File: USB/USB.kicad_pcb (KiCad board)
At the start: 4 copper layers, 70 x 60 mm, 24 parts, among them J1 USBC-4-0-CX90MW9-24P1, U2 ESDA25L, U3 USB SWITCH 2CHANNEL TS3USB221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, U6 usb-polarity-TUSB321RWBR

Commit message: actually connect the test points (DUMBASS)
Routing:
- net MUX POL: track 11.3 -> 108.6 mm
- net USB SWITCH: track 0.00 -> 21.2 mm
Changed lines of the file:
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@@
 	)
 	(segment
+		(start 96.1235 109.5735)
+		(end 85.925 99.375)
+		(width 0.2)
+		(layer "F.Cu")
+		(net "MUX POL")
+	)
+	(segment
+		(start 103.7 75.125)
+		(end 107.79 79.215)
+		(width 0.2)
+		(layer "F.Cu")
+		(net "MUX POL")
+	)
+	(segment
+		(start 89.85 75.125)
+		(end 103.7 75.125)
+		(width 0.2)
+		(layer "F.Cu")
+		(net "MUX POL")
+	)
+	(segment
+		(start 120.63 109.5735)
+		(end 96.1235 109.5735)
+		(width 0.2)
+		(layer "F.Cu")
+		(net "MUX POL")
+	)
+	(segment
 		(start 110.04 92.354857)
 		(end 110.04 91.910001)
@@
 	)
 	(segment
+		(start 85.925 79.05)
+		(end 89.85 75.125)
+		(width 0.2)
+		(layer "F.Cu")
+		(net "MUX POL")
+	)
+	(segment
 		(start 109.756811 92.951)
 		(end 109.081 92.951)
@@
 	)
 	(segment
+		(start 107.79 79.215)
+		(end 107.79 92.15)
+		(width 0.2)
+		(layer "F.Cu")
+		(net "MUX POL")
+	)
+	(segment
 		(start 110.09807 92.412927)
 		(end 110.09807 92.609741)
@@
 		(net "MUX POL")
 	)
+	(segment
+		(start 85.925 99.375)
+		(end 85.925 79.05)
+		(width 0.2)
+		(layer "F.Cu")
+		(net "MUX POL")
+	)
 	(via
 		(at 117.19 92.88)
@@
 		(net "RX1+")
 	)
+	(segment
+		(start 116.8326 99.000001)
+		(end 115.693801 99.000001)
+		(width 0.2)
+		(layer "F.Cu")
+		(net "USB SWITCH")
+	)
+	(segment
+		(start 123.17 101.280199)
+		(end 123.17 109.5735)
+		(width 0.2)
+		(layer "F.Cu")
+		(net "USB SWITCH")
+	)
+	(segment
+		(start 115.405197 98.711397)
+		(end 115.405197 97.738407)
+		(width 0.2)
+		(layer "F.Cu")
+		(net "USB SWITCH")
+	)
+	(segment
+		(start 115.405197 97.738407)
+		(end 116.843604 96.3)
+		(width 0.2)
+		(layer "F.Cu")
+		(net "USB SWITCH")
+	)
+	(segment
+		(start 118.189801 96.3)
+		(end 123.17 101.280199)
+		(width 0.2)
+		(layer "F.Cu")
+		(net "USB SWITCH")
+	)
+	(segment
+		(start 115.693801 99.000001)
+		(end 115.405197 98.711397)
+		(width 0.2)
+		(layer "F.Cu")
+		(net "USB SWITCH")
+	)
+	(segment
+		(start 116.843604 96.3)
+		(end 118.189801 96.3)
+		(width 0.2)
+		(layer "F.Cu")
+		(net "USB SWITCH")
+	)
 	(zone

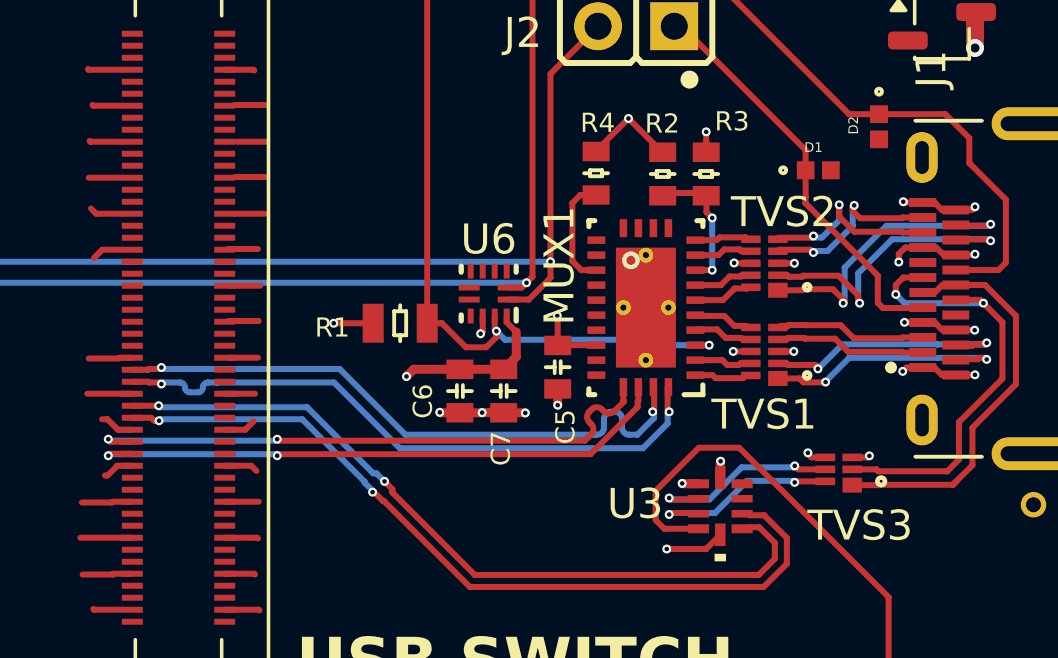
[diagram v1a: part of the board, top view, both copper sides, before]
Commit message: stitching vias along SS lines
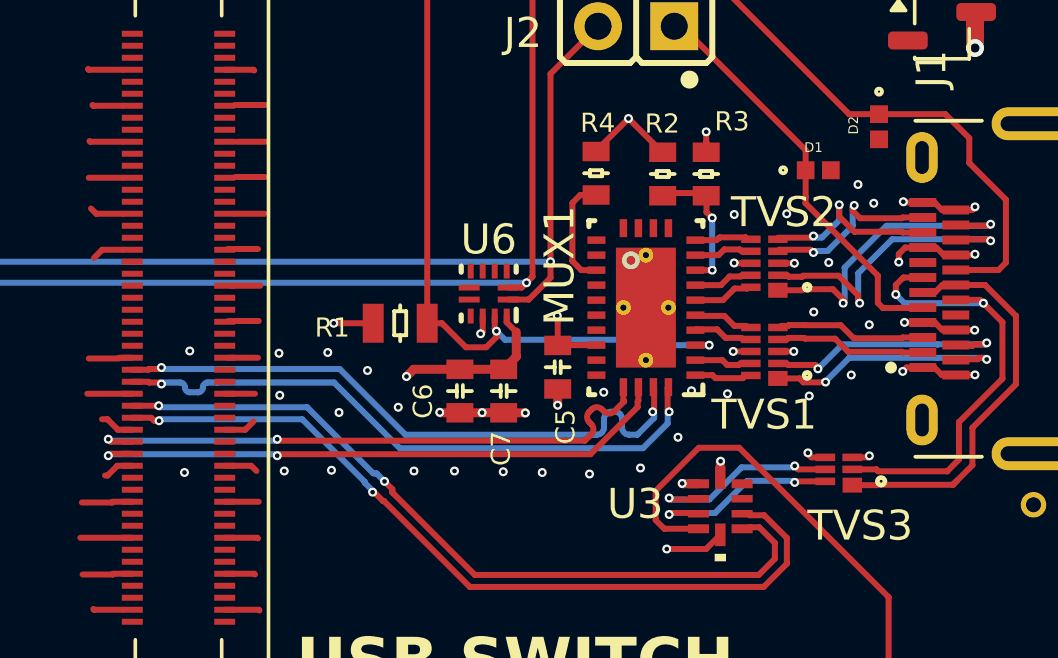
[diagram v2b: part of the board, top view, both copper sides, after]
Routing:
- net GND: vias 18 -> 47
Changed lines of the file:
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@@
+	)
+	(via
+		(at 122.525 92.2)
+		(size 0.3)
+		(drill 0.15)
+		(layers "F.Cu" "B.Cu")
+		(free yes)
+		(net "GND")
 	)
 	(via
@@
 	)
 	(via
+		(at 104.6 97.05)
+		(size 0.3)
+		(drill 0.15)
+		(layers "F.Cu" "B.Cu")
+		(free yes)
+		(net "GND")
+	)
+	(via
+		(at 113.2 97.175)
+		(size 0.3)
+		(drill 0.15)
+		(layers "F.Cu" "B.Cu")
+		(free yes)
+		(net "GND")
+	)
+	(via
+		(at 104.475 93.125)
+		(size 0.3)
+		(drill 0.15)
+		(layers "F.Cu" "B.Cu")
+		(free yes)
+		(net "GND")
+	)
+	(via
+		(at 114.9 96.975)
+		(size 0.3)
+		(drill 0.15)
+		(layers "F.Cu" "B.Cu")
+		(free yes)
+		(net "GND")
+	)
+	(via
+		(at 120.525 94.575)
+		(size 0.3)
+		(drill 0.15)
+		(layers "F.Cu" "B.Cu")
+		(free yes)
+		(net "GND")
+	)
+	(via
+		(at 110.325 97.1)
+		(size 0.3)
+		(drill 0.15)
+		(layers "F.Cu" "B.Cu")
+		(free yes)
+		(net "GND")
+	)
+	(via
+		(at 116.6 94.4)
+		(size 0.3)
+		(drill 0.15)
+		(layers "F.Cu" "B.Cu")
+		(free yes)
+		(net "GND")
+	)
+	(via
+		(at 104.85 95.125)
+		(size 0.3)
+		(drill 0.15)
+		(layers "F.Cu" "B.Cu")
+		(free yes)
+		(net "GND")
+	)
+	(via
+		(at 102.875 94.55)
+		(size 0.3)
+		(drill 0.15)
+		(layers "F.Cu" "B.Cu")
+		(free yes)
+		(net "GND")
+	)
+	(via
 		(at 118.02 90.14)
 		(size 0.3)
@@
 		)
 		(filling no)
+		(net "GND")
+	)
+	(via
+		(at 116.15 95.95)
+		(size 0.3)
+		(drill 0.15)
+		(layers "F.Cu" "B.Cu")
+		(free yes)
 		(net "GND")
 	)
@@
 	)
 	(via
+		(at 99.875 93.075)
+		(size 0.3)
+		(drill 0.15)
+		(layers "F.Cu" "B.Cu")
+		(free yes)
+		(net "GND")
+	)
+	(via
 		(at 117.99 93.09)
 		(size 0.3)
@@
 	)
 	(via
+		(at 106.825 94.95)
+		(size 0.3)
+		(drill 0.15)
+		(layers "F.Cu" "B.Cu")
+		(free yes)
+		(net "GND")
+	)
+	(via
 		(at 109.57 92.5)
 		(size 0.3)
@@
 		)
 		(filling no)
+		(net "GND")
+	)
+	(via
+		(at 119.775 88.5)
+		(size 0.3)
+		(drill 0.15)
+		(layers "F.Cu" "B.Cu")
+		(free yes)
+		(net "GND")
+	)
+	(via
+		(at 113.675 94.45)
+		(size 0.3)
+		(drill 0.15)
+		(layers "F.Cu" "B.Cu")
+		(free yes)
+		(net "GND")
+	)
+	(via
+		(at 122.675 88.15)
+		(size 0.3)
+		(drill 0.15)
+		(layers "F.Cu" "B.Cu")
+		(free yes)
 		(net "GND")
 	)
@@
 	)
 	(via
+		(at 103.025 97.075)
+		(size 0.3)
+		(drill 0.15)
+		(layers "F.Cu" "B.Cu")
+		(free yes)
+		(net "GND")
+	)
+	(via
+		(at 121.925 93.875)
+		(size 0.3)
+		(drill 0.15)
+		(layers "F.Cu" "B.Cu")
+		(free yes)
+		(net "GND")
+	)
+	(via
+		(at 99.7 97.125)
+		(size 0.3)
+		(drill 0.15)
+		(layers "F.Cu" "B.Cu")
+		(free yes)
+		(net "GND")
+	)
+	(via
+		(at 105.8 93.725)
+		(size 0.3)
+		(drill 0.15)
+		(layers "F.Cu" "B.Cu")
+		(free yes)
+		(net "GND")
+	)
+	(via
+		(at 120.675 91.775)
+		(size 0.3)
+		(drill 0.15)
+		(layers "F.Cu" "B.Cu")
+		(free yes)
+		(net "GND")
+	)
+	(via
+		(at 118.025 88.525)
+		(size 0.3)
+		(drill 0.15)
+		(layers "F.Cu" "B.Cu")
+		(free yes)
+		(net "GND")
+	)
+	(via
+		(at 108.7 97.075)
+		(size 0.3)
+		(drill 0.15)
+		(layers "F.Cu" "B.Cu")
+		(free yes)
+		(net "GND")
+	)
+	(via
 		(at 116.29 97.49)
 		(size 0.3)
@@
 	)
 	(via
+		(at 102.85 93.15)
+		(size 0.3)
+		(drill 0.15)
+		(layers "F.Cu" "B.Cu")
+		(free yes)
+		(net "GND")
+	)
+	(via
+		(at 117.8 94.5)
+		(size 0.3)
+		(drill 0.15)
+		(layers "F.Cu" "B.Cu")
+		(free yes)
+		(net "GND")
+	)
+	(via
+		(at 111.625 97.125)
+		(size 0.3)
+		(drill 0.15)
+		(layers "F.Cu" "B.Cu")
+		(free yes)
+		(net "GND")
+	)
+	(via
 		(at 117.57 96.75)
 		(size 0.3)
@@
 	)
 	(via
+		(at 122.15 87.525)
+		(size 0.3)
+		(drill 0.15)
+		(layers "F.Cu" "B.Cu")
+		(free yes)
+		(net "GND")
+	)
+	(via
 		(at 122.53 96.57)
 		(size 0.3)
@@
 	)
 	(via
+		(at 107.35 97.075)
+		(size 0.3)
+		(drill 0.15)
+		(layers "F.Cu" "B.Cu")
+		(free yes)
+		(net "GND")
+	)
+	(via
 		(at 112.14 94.88)
 		(size 0.3)
@@
 		(net "GND")
 	)
+	(via
+		(at 121.175 90.125)
+		(size 0.3)
+		(drill 0.15)
+		(layers "F.Cu" "B.Cu")
+		(free yes)
+		(net "GND")
+	)

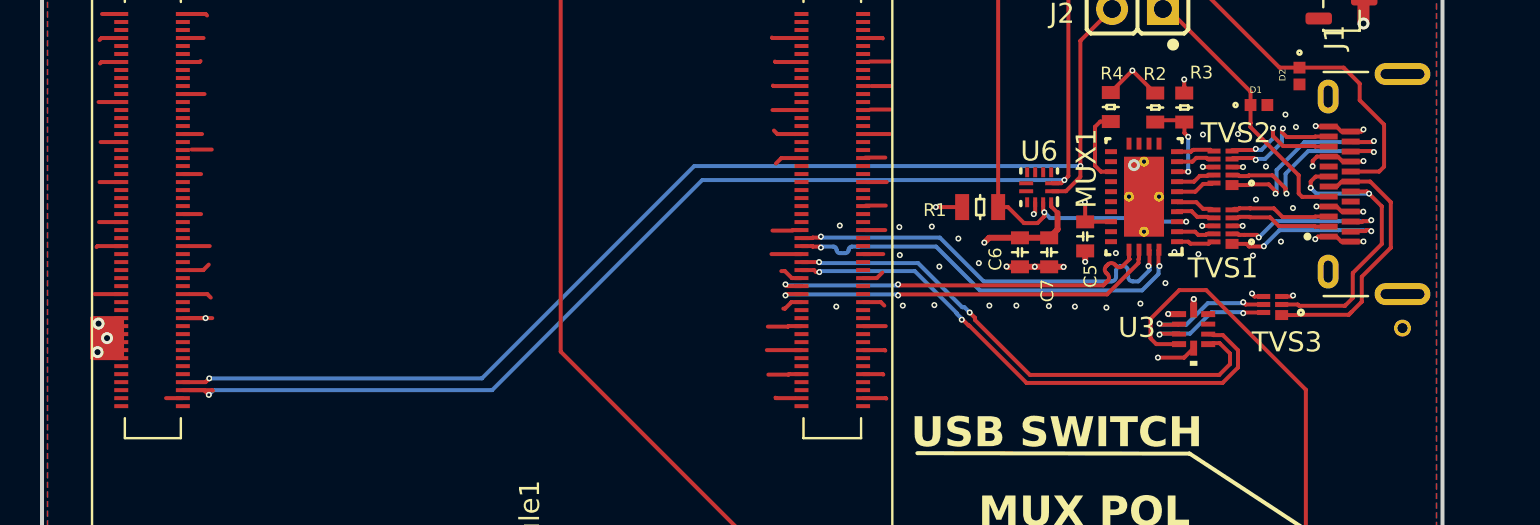
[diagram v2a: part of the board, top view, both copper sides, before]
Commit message: tune and stitch d+,d- lines, connect AGND of type c socket to GND
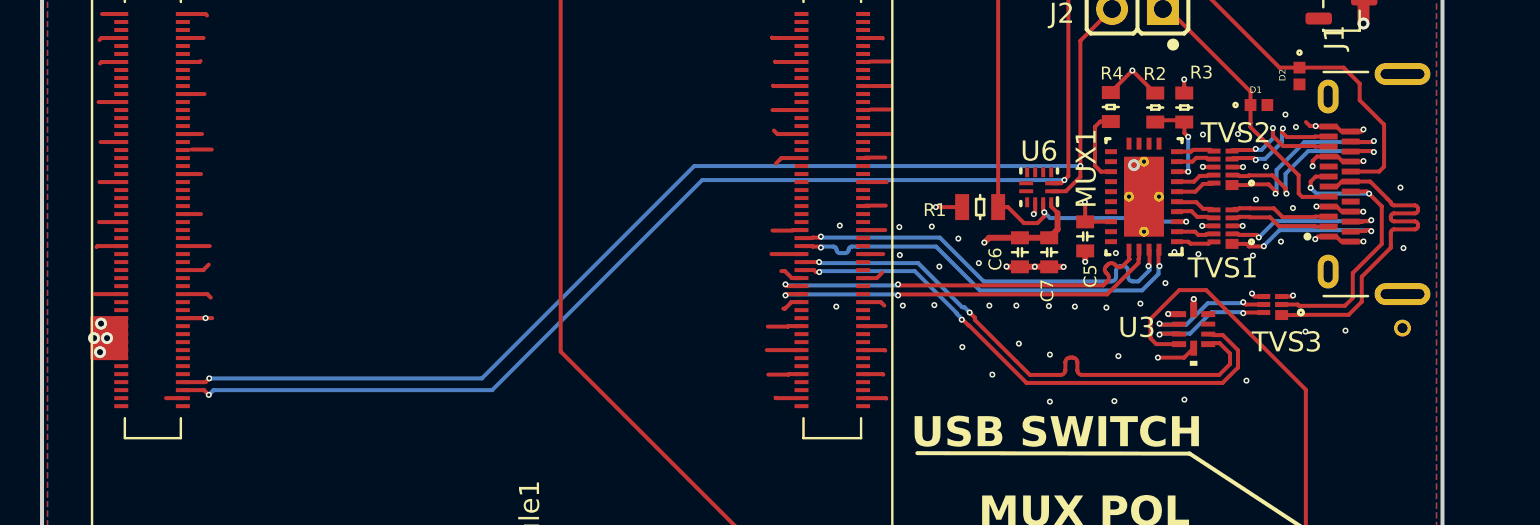
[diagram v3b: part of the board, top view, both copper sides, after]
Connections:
- J1 pad A1: Net-(J1-GND_A) -> GND
- J1 pad A12: Net-(J1-GND_A) -> GND
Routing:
- net D+: track 13.7 -> 18.3 mm
- net SYS D+: track 25.9 -> 27.2 mm
- net CC2-jumpered: track 64.4 -> 63.3 mm
- net GND: track 69.1 -> 69.7 mm, vias 47 -> 60
- net 5V: vias 4 -> 5
